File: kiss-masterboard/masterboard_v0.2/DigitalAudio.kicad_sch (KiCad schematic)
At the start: 15 parts, among them J17 gain_jumper, J18 Speaker, U6 MAX98357, U7 SPH0645LM4H

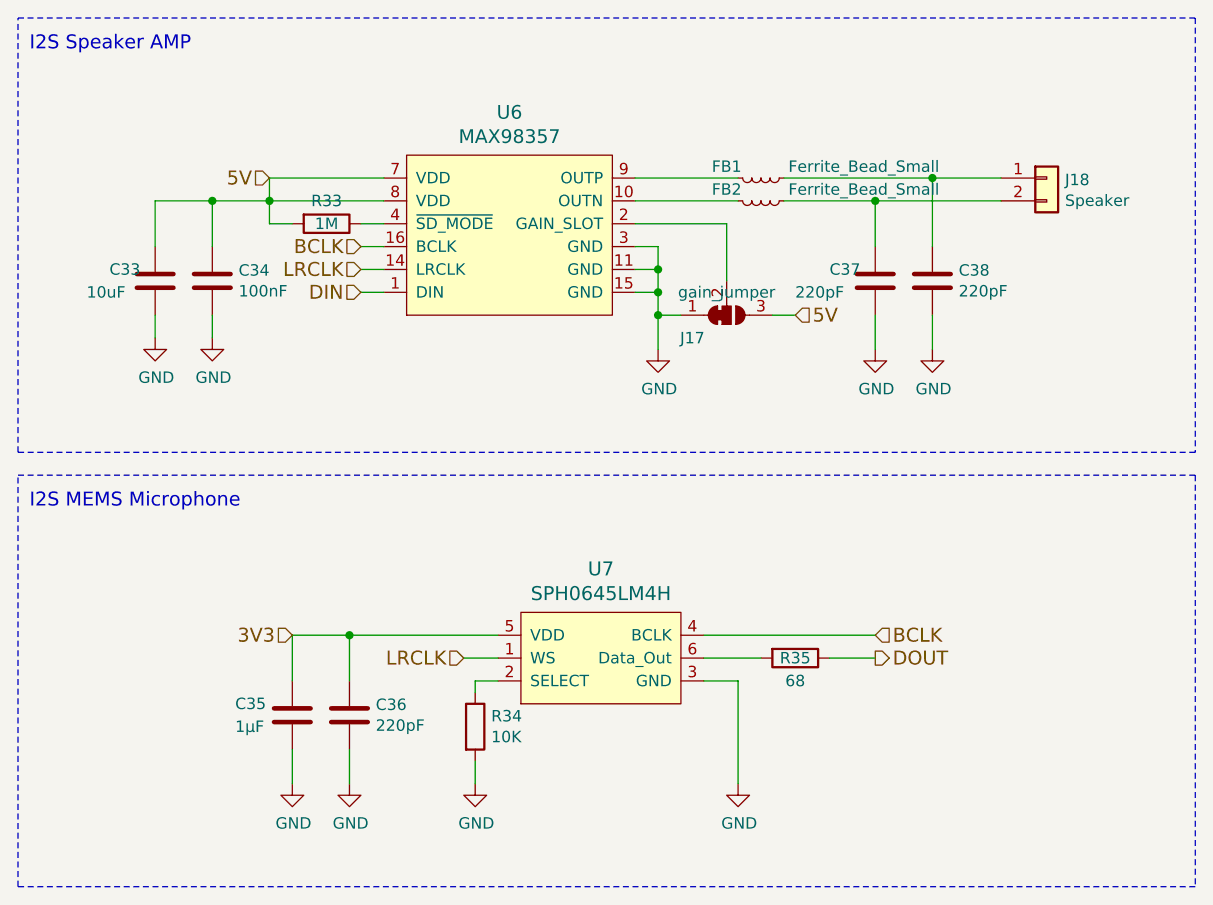
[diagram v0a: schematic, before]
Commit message: replaced symbosl with standart symbols and reduced DRC errorsMAX98357A and TLV75709PDBV symbols
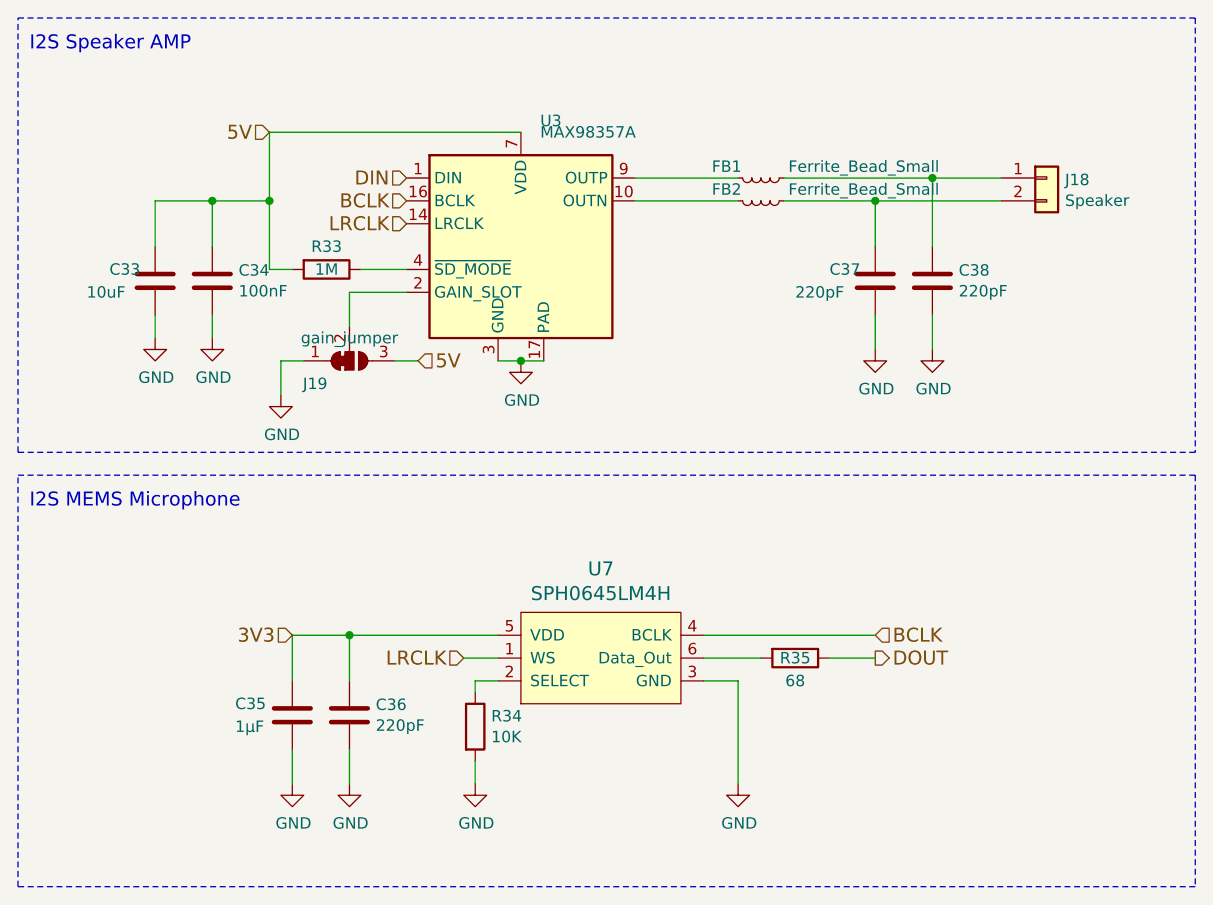
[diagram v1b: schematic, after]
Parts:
- removed J17: gain_jumper, Jumper:SolderJumper-3_P1.3mm_Bridged12_Pad1.0x1.5mm_NumberLabels, symbol Jumper:SolderJumper_3_Bridged12
- removed U6: MAX98357, Package_DFN_QFN:TQFN-16-1EP_3x3mm_P0.5mm_EP1.23x1.23mm, symbol kiss:MAX98357
- added J19: gain_jumper, Jumper:SolderJumper-3_P1.3mm_Bridged12_Pad1.0x1.5mm_NumberLabels, symbol Jumper:SolderJumper_3_Bridged12
- added U3: MAX98357A, Package_DFN_QFN:TQFN-16-1EP_3x3mm_P0.5mm_EP1.23x1.23mm, symbol Audio:MAX98357A
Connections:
- net 5V: now also J19.3 (B), U3.7 (VDD), U3.8 (VDD)
- net BCLK: now also U3.16 (BCLK)
- net DIN: now also U3.1 (DIN)
- net GND: now also J19.1 (A), U3.11 (GND), U3.15 (GND), U3.17 (PAD), U3.3 (GND)
- net LRCLK: now also U3.14 (LRCLK)
- net at FB2.2: now also U3.10 (OUTN)
- net at R33.1: now also U3.4 (~{SD_MODE})
- net at FB1.2: now also U3.9 (OUTP)
- new net: J19.2 (C), U3.2 (GAIN_SLOT)
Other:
- moved on the sheet: R33

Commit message: Adjust to new batterypack,
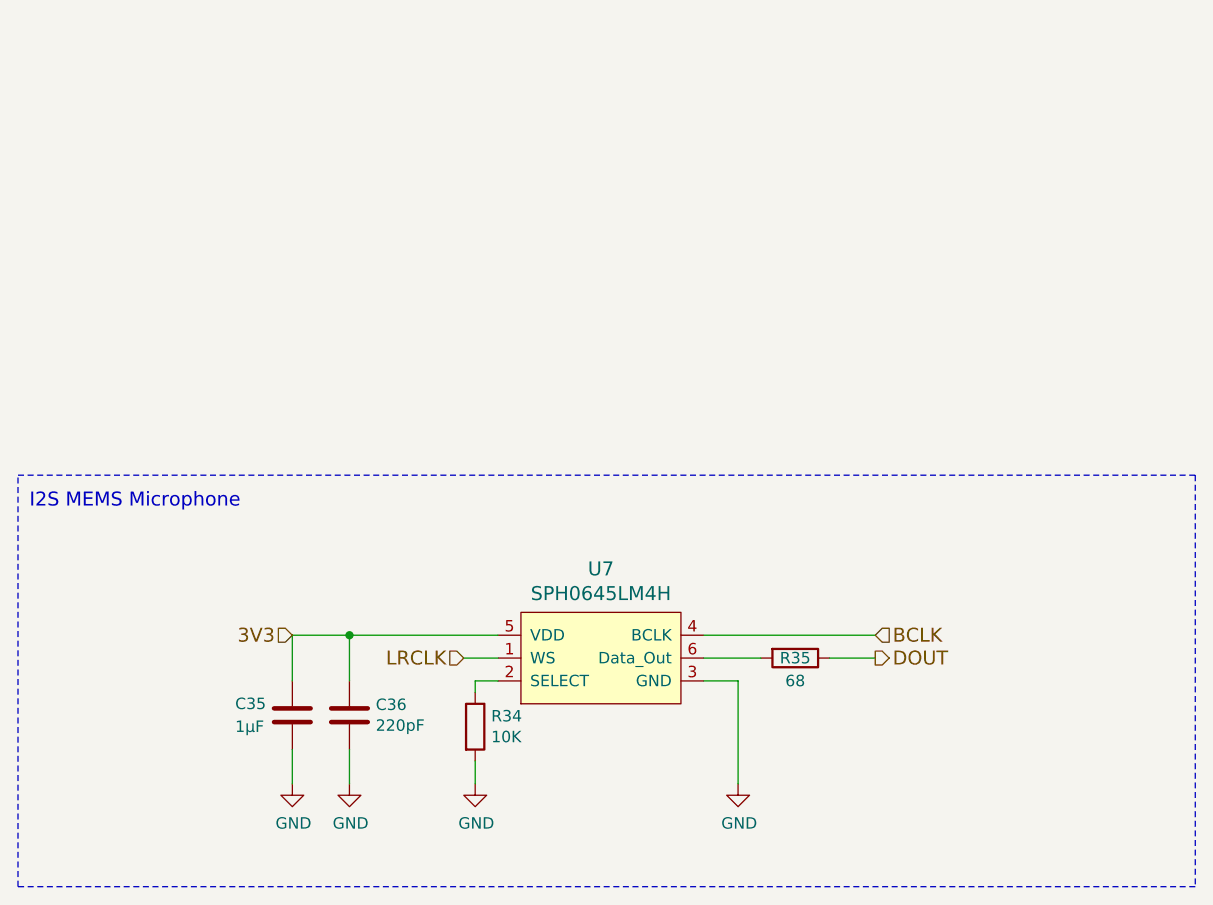
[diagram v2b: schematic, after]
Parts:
- removed C33: 10uF, Capacitor_SMD:C_0603_1608Metric, symbol Device:C
- removed C34: 100nF, Capacitor_SMD:C_0603_1608Metric, symbol Device:C
- removed C37, C38: 220pF, Capacitor_SMD:C_0603_1608Metric, symbol Device:C
- removed FB1, FB2: Ferrite_Bead_Small, Inductor_SMD:L_0603_1608Metric, symbol Device:L_Small
- removed J18: Speaker, Connector_PinHeader_2.54mm:PinHeader_1x02_P2.54mm_Vertical, symbol Connector_Generic:Conn_01x02
- removed J19: gain_jumper, Jumper:SolderJumper-3_P1.3mm_Bridged12_Pad1.0x1.5mm_NumberLabels, symbol Jumper:SolderJumper_3_Bridged12
- removed R33: 1M, Resistor_SMD:R_0603_1608Metric, symbol Device:R
- removed U3: MAX98357A, Package_DFN_QFN:TQFN-16-1EP_3x3mm_P0.5mm_EP1.23x1.23mm, symbol Audio:MAX98357A
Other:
- note removed: "I2S Speaker AMP"

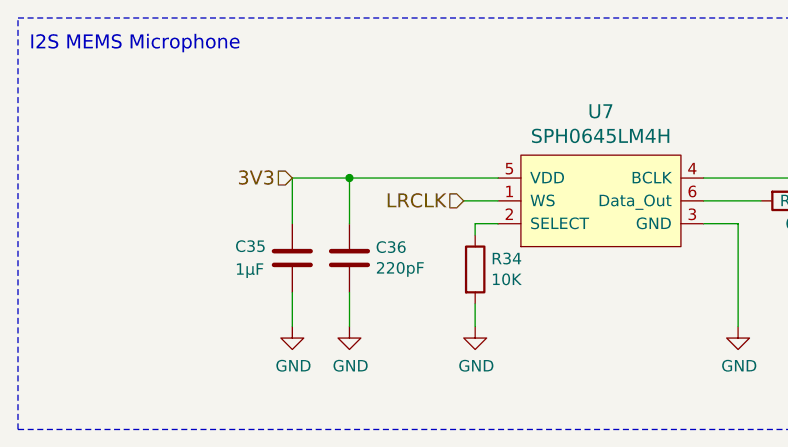
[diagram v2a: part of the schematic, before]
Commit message: Added IMU, routed extension layer, switched battery polarity
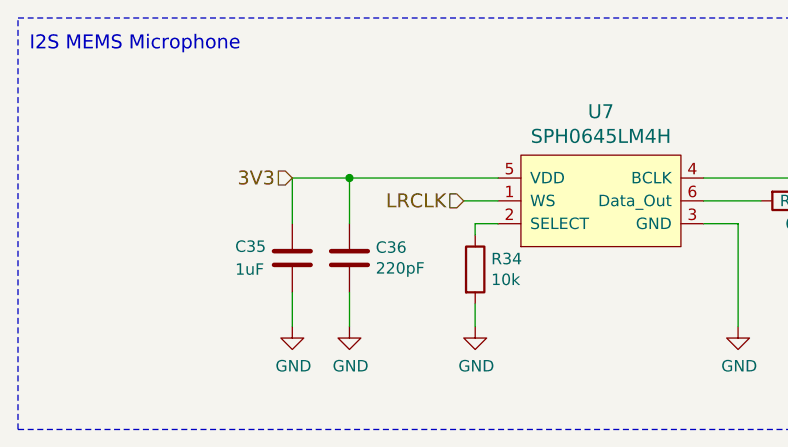
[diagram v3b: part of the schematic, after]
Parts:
- C35: value 1µF -> 1uF
- R34: value 10K -> 10k
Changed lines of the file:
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@@
 			)
 		)
-		(property "Value" "10K"
+		(property "Value" "10k"
 			(at 67.818 95.123 0)
 			(show_name no)
@@
 			)
 		)
-		(property "Value" "1µF"
+		(property "Value" "1uF"
 			(at 39.37 93.98 0)
 			(show_name no)

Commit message: add cnumbers initial order v04a
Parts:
- C35: JLCNR (none) -> C15849
- C36: JLCNR (none) -> C1603
- R34: JLCNR (none) -> C25804
- R35: JLCNR (none) -> C27592
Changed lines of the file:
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@@
+			)
+		)
+		(property "JLCNR" ""
+			(at 80.01 86.36 0)
+			(hide yes)
+			(show_name no)
+			(do_not_autoplace no)
+			(effects
+				(font
+					(size 3.9878 3.9878)
+				)
 			)
 		)
@@
 			)
 		)
+		(property "JLCNR" "C25804"
+			(at 66.04 93.98 0)
+			(hide yes)
+			(show_name no)
+			(do_not_autoplace no)
+			(effects
+				(font
+					(size 3.9878 3.9878)
+				)
+			)
+		)
 		(pin "1"
 		)
@@
 			)
 		)
+		(property "JLCNR" "C27592"
+			(at 101.6 86.36 90)
+			(hide yes)
+			(show_name no)
+			(do_not_autoplace no)
+			(effects
+				(font
+					(size 3.9878 3.9878)
+				)
+			)
+		)
 		(pin "1"
 		)
@@
 			)
 		)
+		(property "JLCNR" "C15849"
+			(at 45.72 92.71 0)
+			(hide yes)
+			(show_name no)
+			(do_not_autoplace no)
+			(effects
+				(font
+					(size 3.9878 3.9878)
+				)
+			)
+		)
 		(pin "1"
 		)
@@
 				)
 			)
+		)
+		(property "JLCNR" "C1603"
+			(at 52.07 92.71 0)
+			(hide yes)
+			(show_name no)
+			(do_not_autoplace no)
+			(effects
+				(font
+					(size 3.9878 3.9878)
+				)
+			)
